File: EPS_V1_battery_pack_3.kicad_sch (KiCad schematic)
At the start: 33 parts, among them U1 MP2672AGD-0000-Z, U5 MAX17205G+

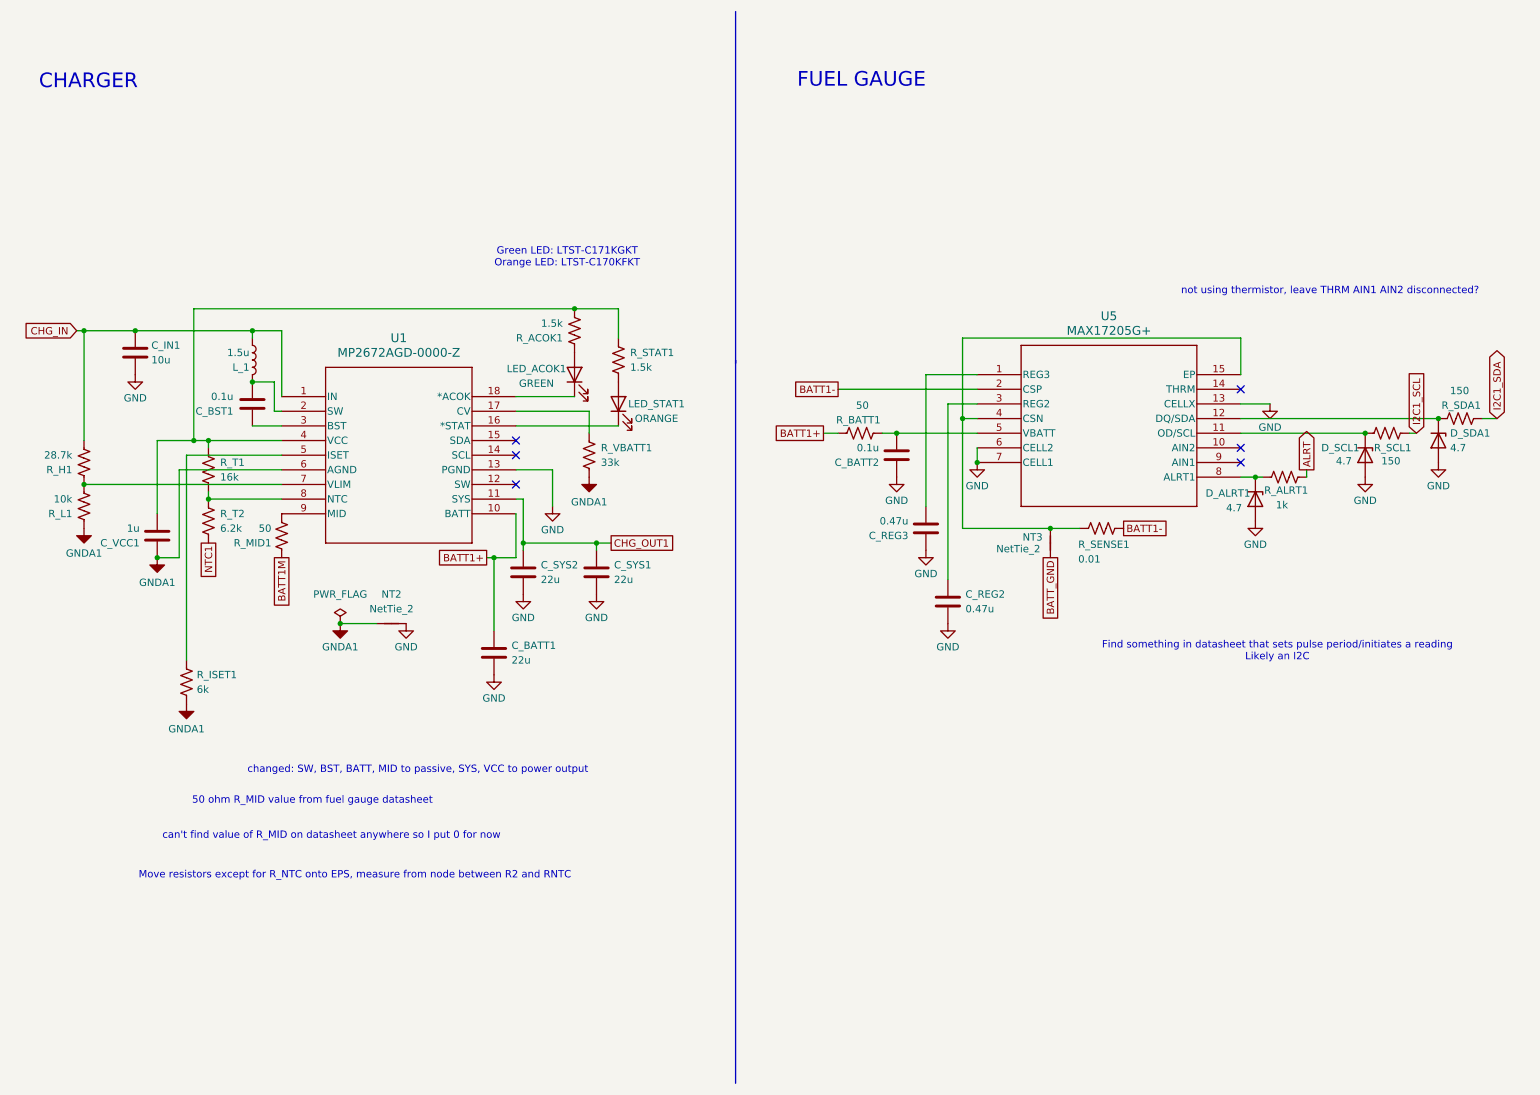
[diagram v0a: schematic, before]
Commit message: Add other battery packs, connect all ALRT signals, assign footprints for new components, make inhibit switch footprints
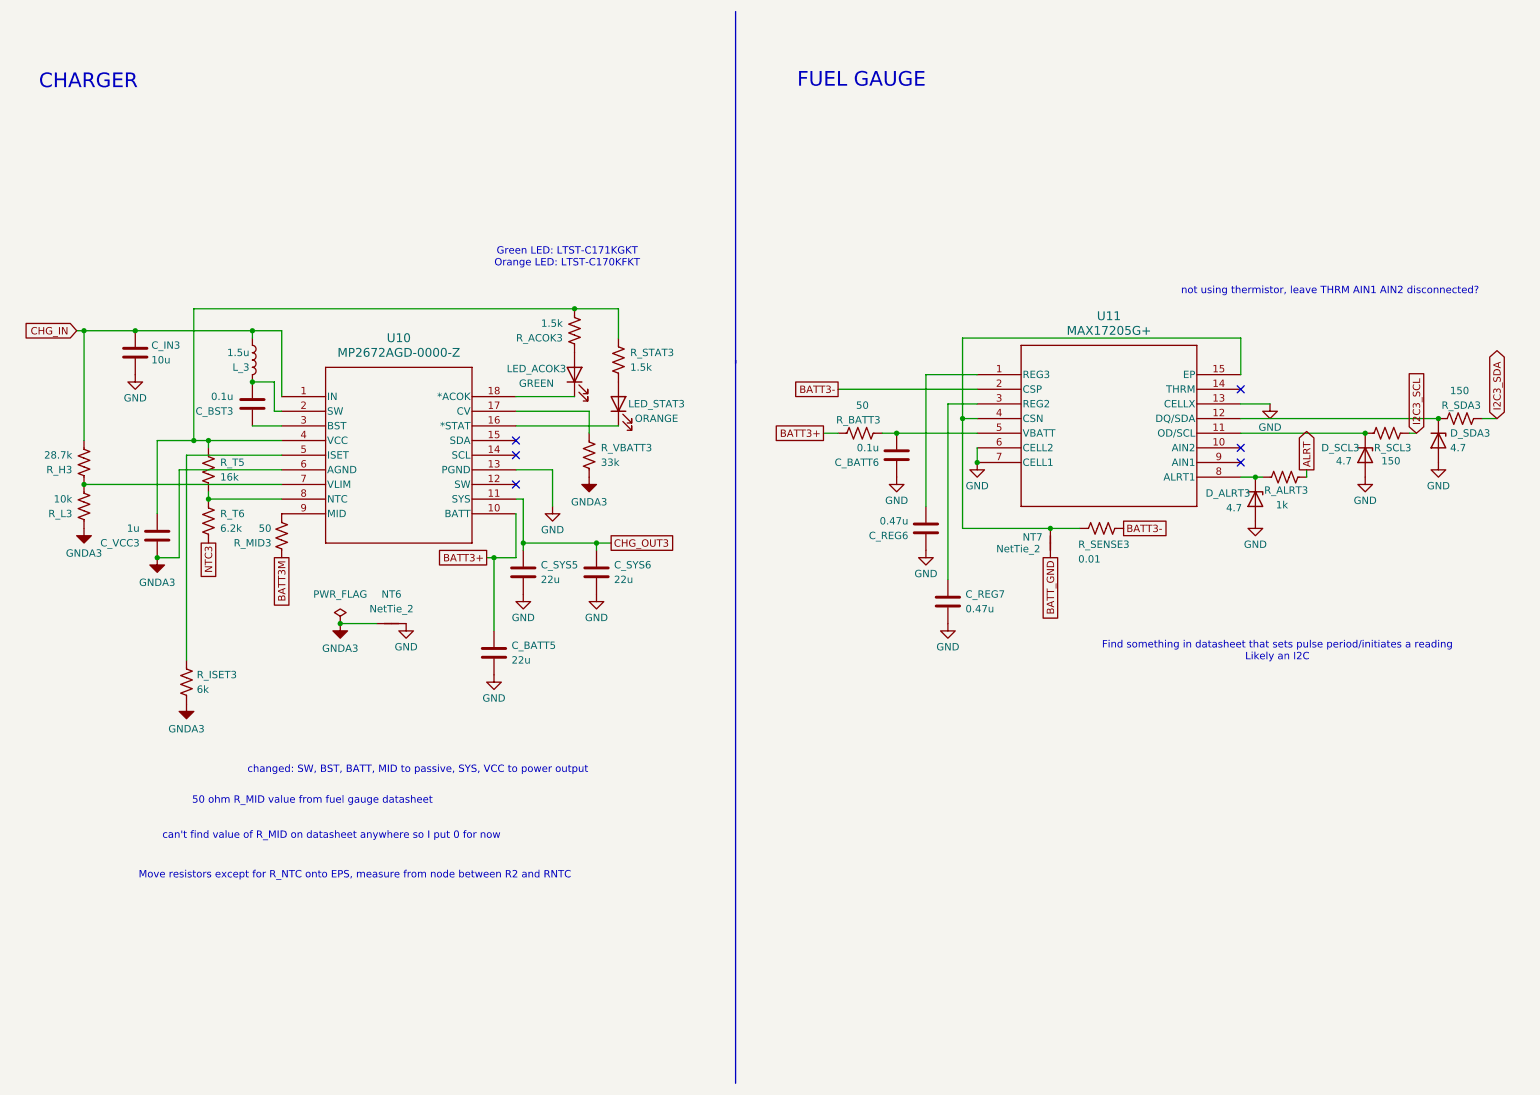
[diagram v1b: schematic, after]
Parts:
- removed C_BATT1, C_SYS1, C_SYS2: 22u, Capacitor_SMD:C_0805_2012Metric, symbol Device:C
- removed C_BATT2, C_BST1: 0.1u, Capacitor_SMD:C_0603_1608Metric, symbol Device:C
- removed C_IN1: 10u, Capacitor_SMD:C_0805_2012Metric, symbol Device:C
- removed C_REG2, C_REG3: 0.47u, Capacitor_SMD:C_0603_1608Metric, symbol Device:C
- removed C_VCC1: 1u, Capacitor_SMD:C_0603_1608Metric, symbol Device:C
- removed D_ALRT1, D_SCL1, D_SDA1: 4.7, Diode_SMD:D_0603_1608Metric, symbol Device:D_Zener
- removed LED_ACOK1: GREEN, LED_SMD:LED_0805_2012Metric, symbol Device:LED
- removed LED_STAT1: ORANGE, LED_SMD:LED_0805_2012Metric, symbol Device:LED
- removed L_1: 1.5u, AMELA2012S_1R5MT:IND_AMELA2012S-1R5MT, symbol Device:L
- removed NT2, NT3: NetTie_2, NetTie:NetTie-2_SMD_Pad2.0mm, symbol Device:NetTie_2
- removed R_ACOK1, R_STAT1: 1.5k, Resistor_SMD:R_0603_1608Metric, symbol Device:R_US
- removed R_ALRT1: 1k, Resistor_SMD:R_0603_1608Metric, symbol Device:R_US
- removed R_BATT1, R_MID1: 50, Resistor_SMD:R_0603_1608Metric, symbol Device:R_US
- removed R_H1: 28.7k, Resistor_SMD:R_0603_1608Metric, symbol Device:R_US
- removed R_ISET1: 6k, Resistor_SMD:R_0603_1608Metric, symbol Device:R_US
- removed R_L1: 10k, Resistor_SMD:R_0603_1608Metric, symbol Device:R_US
- removed R_SCL1, R_SDA1: 150, Resistor_SMD:R_0603_1608Metric, symbol Device:R_US
- removed R_SENSE1: 0.01, Resistor_SMD:R_0603_1608Metric, symbol Device:R_US
- removed R_T1: 16k, Resistor_SMD:R_0603_1608Metric, symbol Device:R_US
- removed R_T2: 6.2k, Resistor_SMD:R_0603_1608Metric, symbol Device:R_US
- removed R_VBATT1: 33k, Resistor_SMD:R_0603_1608Metric, symbol Device:R_US
- removed U1: MP2672AGD-0000-Z, MP2672AGD_0000_Z:QFN-18_MP2672A_MNP, symbol 2026-04-14_17-23-40:MP2672AGD-0000-Z
- removed U5: MAX17205G+, MAX17205G:21-0137_T1433&plus_2C_MXM, symbol MAX17205G:MAX17205G+
- added C_BATT5, C_SYS5, C_SYS6: 22u, Capacitor_SMD:C_0805_2012Metric, symbol Device:C
- added C_BATT6, C_BST3: 0.1u, Capacitor_SMD:C_0603_1608Metric, symbol Device:C
- added C_IN3: 10u, Capacitor_SMD:C_0805_2012Metric, symbol Device:C
- added C_REG6, C_REG7: 0.47u, Capacitor_SMD:C_0603_1608Metric, symbol Device:C
- added C_VCC3: 1u, Capacitor_SMD:C_0603_1608Metric, symbol Device:C
- added D_ALRT3, D_SCL3, D_SDA3: 4.7, Diode_SMD:D_0603_1608Metric, symbol Device:D_Zener
- added LED_ACOK3: GREEN, LED_SMD:LED_0805_2012Metric, symbol Device:LED
- added LED_STAT3: ORANGE, LED_SMD:LED_0805_2012Metric, symbol Device:LED
- added L_3: 1.5u, AMELA2012S_1R5MT:IND_AMELA2012S-1R5MT, symbol Device:L
- added NT6, NT7: NetTie_2, NetTie:NetTie-2_SMD_Pad2.0mm, symbol Device:NetTie_2
- added R_ACOK3, R_STAT3: 1.5k, Resistor_SMD:R_0603_1608Metric, symbol Device:R_US
- added R_ALRT3: 1k, Resistor_SMD:R_0603_1608Metric, symbol Device:R_US
- added R_BATT3, R_MID3: 50, Resistor_SMD:R_0603_1608Metric, symbol Device:R_US
- added R_H3: 28.7k, Resistor_SMD:R_0603_1608Metric, symbol Device:R_US
- added R_ISET3: 6k, Resistor_SMD:R_0603_1608Metric, symbol Device:R_US
- added R_L3: 10k, Resistor_SMD:R_0603_1608Metric, symbol Device:R_US
- added R_SCL3, R_SDA3: 150, Resistor_SMD:R_0603_1608Metric, symbol Device:R_US
- added R_SENSE3: 0.01, Resistor_SMD:R_0603_1608Metric, symbol Device:R_US
- added R_T5: 16k, Resistor_SMD:R_0603_1608Metric, symbol Device:R_US
- added R_T6: 6.2k, Resistor_SMD:R_0603_1608Metric, symbol Device:R_US
- added R_VBATT3: 33k, Resistor_SMD:R_0603_1608Metric, symbol Device:R_US
- added U10: MP2672AGD-0000-Z, MP2672AGD_0000_Z:QFN-18_MP2672A_MNP, symbol 2026-04-14_17-23-40:MP2672AGD-0000-Z
- added U11: MAX17205G+, MAX17205G:21-0137_T1433&plus_2C_MXM, symbol MAX17205G:MAX17205G+
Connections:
- net ALRT: now also R_ALRT3.2
- net BATT_GND: now also NT7.1
- net CHG_IN: now also C_IN3.1, L_3.1, R_H3.2, U10.1 (IN)
- net GND: now also C_BATT5.2, C_BATT6.1, C_IN3.2, C_REG6.1, C_REG7.2, C_SYS5.2, C_SYS6.2, D_ALRT3.2 (A), D_SCL3.2 (A), D_SDA3.2 (A), NT6.2, U10.13 (PGND), U11.13 (CELLX), U11.6 (CELL2), U11.7 (CELL1)
- new net: C_BATT6.2, R_BATT3.2, U11.5 (VBATT)
- new net: C_VCC3.2, R_ACOK3.2, R_STAT3.1, R_T5.1, U10.4 (VCC)
- new net: LED_STAT3.2 (A), R_STAT3.2
- new net: D_SCL3.1 (K), R_SCL3.1, U11.11 (OD/SCL)
- new net: D_SDA3.1 (K), R_SDA3.1, U11.12 (DQ/SDA)
- new net: R_T5.2, R_T6.1, U10.8 (NTC)
- new net: R_MID3.2, U10.9 (MID)
- new net: C_REG6.2, U11.1 (REG3)
- new net: D_ALRT3.1 (K), R_ALRT3.1, U11.8 (ALRT1)
- new net: NT7.2, R_SENSE3.2, U11.15 (EP), U11.4 (CSN)
- new net: LED_STAT3.1 (K), U10.16 (*STAT)
- new net: R_VBATT3.1, U10.17 (CV)
- new net: LED_ACOK3.1 (K), U10.18 (*ACOK)
- new net: C_BST3.2, L_3.2, U10.2 (SW)
- new net: C_BST3.1, U10.3 (BST)
- new net: R_ISET3.1, U10.5 (ISET)
- new net: R_H3.1, R_L3.2, U10.7 (VLIM)
- new net: C_REG7.1, U11.3 (REG2)
- new net: LED_ACOK3.2 (A), R_ACOK3.1
- new net BATT3+: C_BATT5.1, R_BATT3.1, U10.10 (BATT)
- new net BATT3-: R_SENSE3.1, U11.2 (CSP)
- new net BATT3M: R_MID3.1
- new net CHG_OUT3: C_SYS5.1, C_SYS6.1, U10.11 (SYS)
- new net GNDA3: C_VCC3.1, NT6.1, R_ISET3.2, R_L3.1, R_VBATT3.2, U10.6 (AGND)
- new net I2C3_SCL: R_SCL3.2
- new net I2C3_SDA: R_SDA3.2
- new net NTC3: R_T6.2

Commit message: Do layout draft
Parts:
- removed D_ALRT3: 4.7, Diode_SMD:D_0603_1608Metric, symbol Device:D_Zener
- removed R_ALRT3: 1k, Resistor_SMD:R_0603_1608Metric, symbol Device:R_US
- NT6, NT7: footprint NetTie:NetTie-2_SMD_Pad2.0mm -> NetTie:NetTie-2_SMD_Pad0.5mm
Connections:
- net ALRT: now also U11.8 (ALRT1)
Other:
- moved on the sheet: D_SCL3, D_SDA3, R_SCL3, R_SDA3
